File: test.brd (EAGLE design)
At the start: 28.9 x 20.9 mm, 17 parts

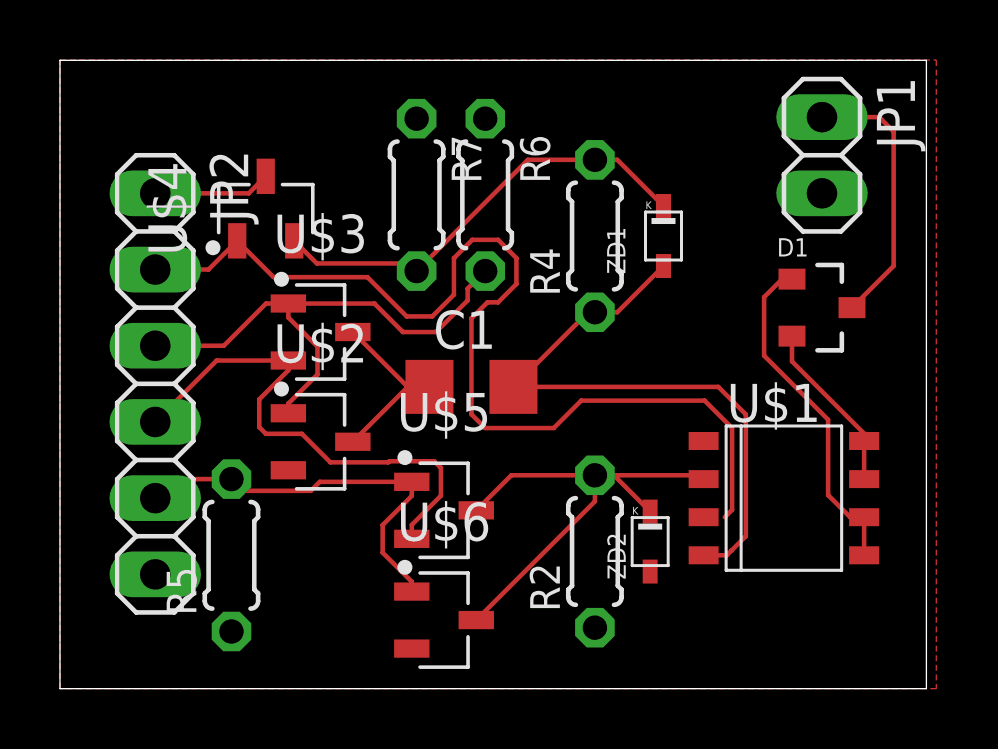
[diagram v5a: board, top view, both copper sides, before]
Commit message: added cmos designed fet driver
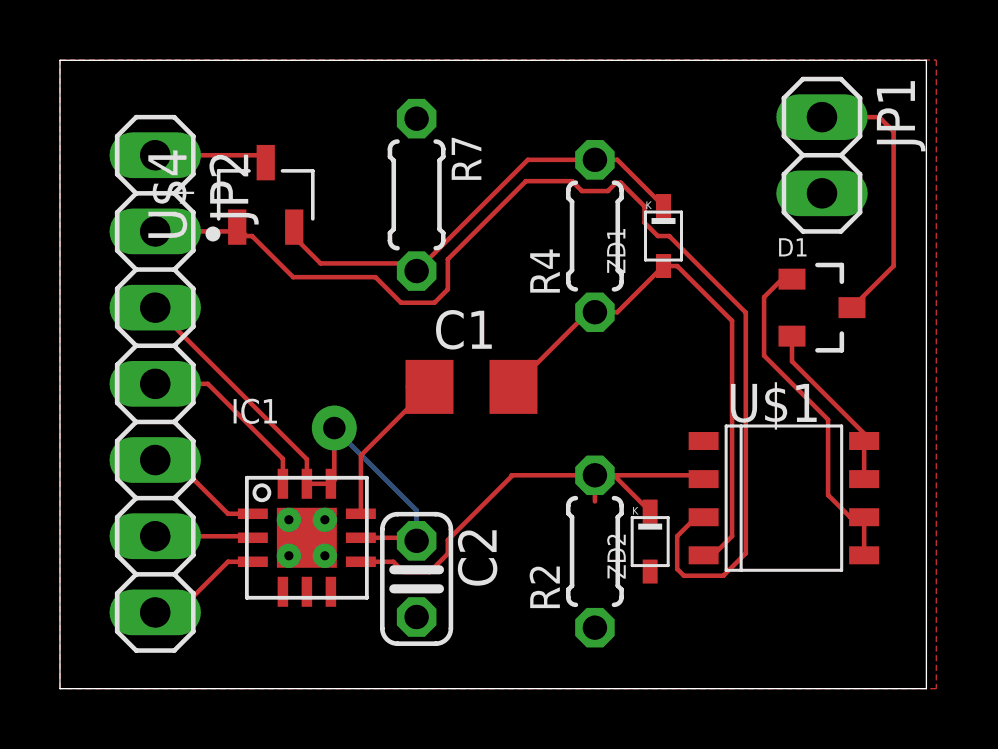
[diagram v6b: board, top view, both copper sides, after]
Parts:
- removed R5, R6: 103, rcl:0204/5
- removed U$2, U$6: IRLML6344TRPBFTR, Transistor-FET:SOT95P250X120-3
- removed U$3, U$5: IRLML2246TRPBFTR, Transistor-FET:SOT95P250X120-3
- added C2: 474, rcl:C025-024X044
- added IC1: MD1213K6, md1213:QFN12
- JP2: device pinhead:1X06 -> pinhead:1X07
- moved U$4 0.46 mm to (6.86, 16.5)
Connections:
- new net N$10: IC1.3, JP2.7
- net +12V: now also C2.1, IC1.10, IC1.11, IC1.8, JP2.3; no longer JP2.4, U$3.2, U$5.2
- net GND: now also C2.2, IC1.2, IC1.4, IC1.5, IC1.6, IC1.THP, IC1.THV$1, IC1.THV$2, IC1.THV$3, IC1.THV$4; no longer R5.1, R6.1, U$2.2, U$6.2
- net N$1: now also IC1.7; no longer U$5.3, U$6.3
- net N$2: now also IC1.9; no longer U$2.3, U$3.3
- net N$4: now also IC1.1; no longer R5.2, U$5.1, U$6.1
- net N$5: now also IC1.12, JP2.4; no longer JP2.3, R6.2, U$2.1, U$3.1
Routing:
- net N$5: track 17.5 -> 6.12 mm
- net N$4: track 13.6 -> 4.00 mm
- net VPP: track 34.2 -> 38.4 mm
- net N$10: track 0.00 -> 3.95 mm
- net GND: track 0.00 -> 3.28 mm
- net N$3: track 20.5 -> 18.1 mm
- net +12V: vias 0 -> 1

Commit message: modified a value of 300V source symbol; Having a ploblem probably caused by Capacitor which require 240ms to charge
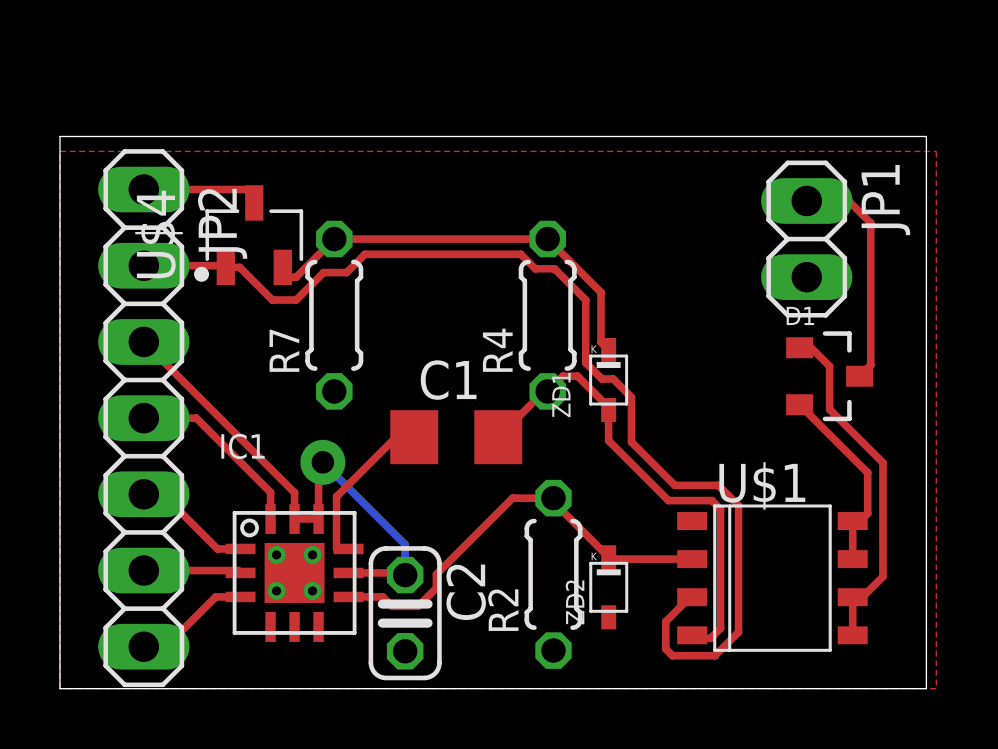
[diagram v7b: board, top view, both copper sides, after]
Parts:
- moved ZD1 5.14 mm to (18.3, 10.3)
- moved R7 4.86 mm to (9.14, 12.4), turned to 90 degrees
- moved R4 3.08 mm to (16.3, 12.4)
- moved JP1 2.84 mm to (24.9, 15.0)
- moved U$1 2.69 mm to (23.7, 3.68)
- moved D1 2.30 mm to (25.7, 10.4)
- moved ZD2 2.06 mm to (18.3, 3.38)
- moved C1 1.75 mm to (13.2, 8.38)
- moved R2 1.58 mm to (16.4, 3.81)
- moved U$4 1.40 mm to (6.48, 15.1)
- moved IC1 1.24 mm to (7.82, 3.86)
- moved JP2 1.20 mm to (2.79, 9.02)
- moved C2 1.20 mm to (11.5, 2.51)
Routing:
- net VPP: track 38.4 -> 35.7 mm
- net N$3: track 18.1 -> 15.8 mm
- net N$1: track 16.5 -> 14.3 mm
- net N$9: track 9.03 -> 7.70 mm
- net N$6: track 15.3 -> 14.2 mm
- net N$8: track 5.76 -> 6.44 mm
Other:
- board size 28.9 x 20.9 mm -> 28.9 x 18.4 mm
